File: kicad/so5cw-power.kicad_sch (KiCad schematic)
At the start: 132 parts, among them J1 Screw_Terminal_01x02, J2 Screw_Terminal_01x02, J3 Screw_Terminal_01x02, J4 Screw_Terminal_01x02, J5 Screw_Terminal_01x02, J6 Raspberry Pi Zero 2W, J7 Screw_Terminal_01x02, J8 Screw_Terminal_01x02, J9 Screw_Terminal_01x02, K1 G2RL-1A-E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

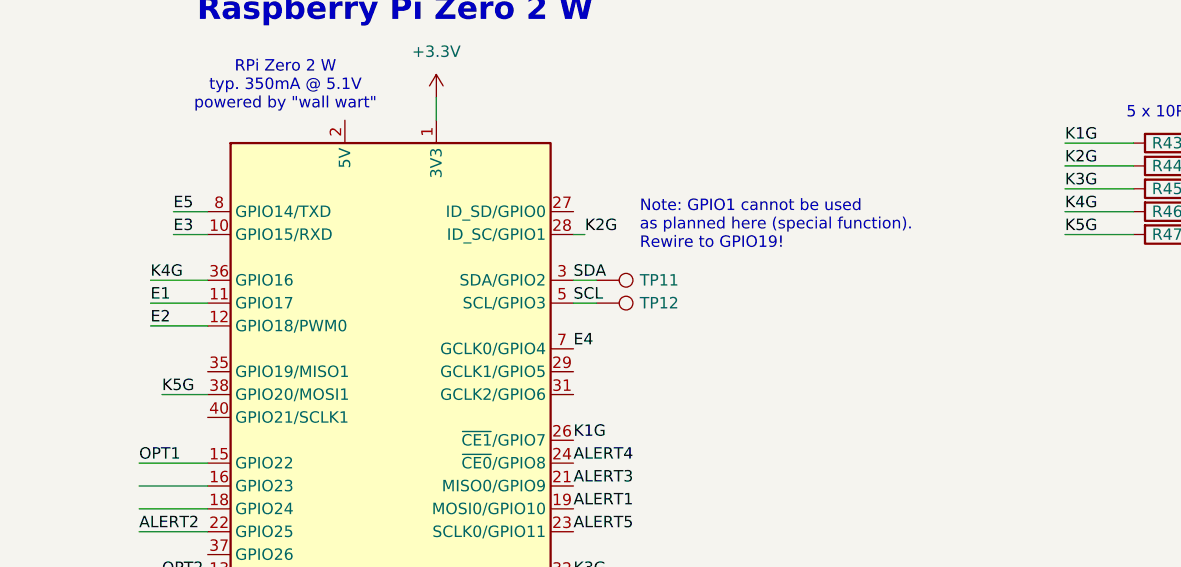
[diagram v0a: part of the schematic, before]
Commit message: Connect Relay K2 to GPIO19, because GPIO1 is reserved
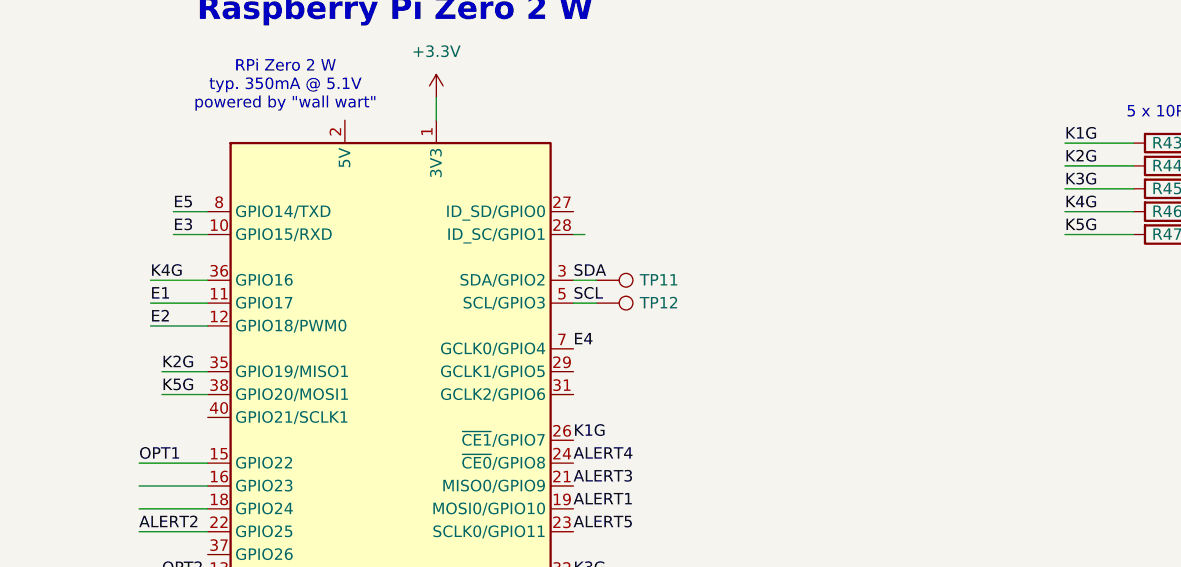
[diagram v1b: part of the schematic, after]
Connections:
- net K2G: now also J6.35 (GPIO19/MISO1); no longer J6.28 (ID_SC/GPIO1)
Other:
- note removed: "Note: GPIO1 cannot be used as planned here (special function). Rewire to GPIO19!"
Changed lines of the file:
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@@
 		(company "DJ5CW / SO5CW")
 	)
-	(text "Note: GPIO1 cannot be used\nas planned here (special function).\nRewire to GPIO19!"
-		(exclude_from_sim no)
-		(at 281.686 208.534 0)
-		(effects
-			(font
-				(size 1.27 1.27)
-			)
-			(justify left)
-		)
-	)
 	(text "13.8V DC\nOutput 2\n(Band Dec.)"
 		(exclude_from_sim no)
@@
 	(wire
 		(pts
+			(xy 228.6 224.79) (xy 233.68 224.79)
+		)
+		(stroke
+			(width 0)
+			(type default)
+		)
+	)
+	(wire
+		(pts
 			(xy 346.71 58.42) (xy 344.17 58.42)
 		)
@@
 		)
 	)
+	(label "K2G"
+		(at 228.6 224.79 0)
+		(effects
+			(font
+				(size 1.27 1.27)
+			)
+			(justify left bottom)
+		)
+	)
 	(label "ALERT2"
 		(at 363.22 109.22 0)
@@
 		(effects
 			(font
-				(size 1.27 1.27)
-			)
-			(justify left bottom)
-		)
-	)
-	(label "K2G"
-		(at 275.59 209.55 0)
-		(effects
-			(font

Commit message: Version 1.1 (K2 re-routed from GPIO1 to GPIO19). Cosmetics.
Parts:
- R55, R56: value 5k6 -> 2k2
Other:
- moved on the sheet: D16, FID1, J6, J7, J8, J9, R53, R55, R56, R57, R58, TP11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

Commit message: schematic: rearrange outputs (1..5) and adjust descriptions
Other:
- note added: "Output 1 13.8V"
- note added: "Output 2 13.8V"
- note added: "Output 3 5V (reg.)"
- note added: "Output 4 13.8V"
- note added: "Output 5 13.8V"
- note removed: "13.8V DC Output 1 (ATU)"
- note removed: "13.8V DC Output 2 (Band Dec.)"
- note removed: "13.8V DC Output 3 (RRC-1128)"
- note removed: "13.8V DC Output 4 (misc.)"
- note removed: "5V DC Output (Switch)"
- moved on the sheet: C1, C10, C14, C15, C16, C3, C5, C6, C7, C9, D10, D2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
